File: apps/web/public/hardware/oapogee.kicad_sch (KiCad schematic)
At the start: 22 parts, among them J1 USB-C-16P, J2 S2B-PH-K-S, J3 ANT-902-928, U1 MCP73831, U2 TODO-BUCK-BOOST, U3 RP2350A, U4 W25Q128JVSIQ, U5 BMP390, U6 ICM-42688-P, U7 ADXL375, U8 SX1262, U9 MAX-M10S

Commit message: Fix 37 audited defects, wire the board's power, and make zoom crisp
A four-way audit with adversarial verification found 37 confirmed defects, seven
of them blockers. The verifier's job was to refute each finding, so what
survived is what could be proven from the files.

Specs. The STATUS pressure field's stated range did not follow from its own
encoding formula and matched no consistent reading of it, so two implementers
would have clamped and raised BARO_FAULT at different pressures. It is now
whole pascals offset by 50000, which covers 50000 to 115535 Pa in exactly 65536
codes, makes the "offset so it fits in 16 bits" rationale literally true, and
puts the packet and the log on the same pressure scale. The reference decoder
silently dropped the body of two of the five packet types, including the BEACON
that carries the apogee figure; it now covers all five. t_ms before arming,
POSITION with no fix, and the manifest summary's absent-versus-null
contradiction are all defined rather than left to the reader.

Content. The claim that an IMU saturates "around 16 g" above "a C motor" was
stated as fact in six rendered places while the part's own note admitted the
threshold had never been computed. The mechanism stays, because it is real and
worth explaining; the specific figures are now marked. Same for a stray range
figure of "a kilometre" on a site that says it publishes no range figures.

Hardware. The schematic had no GND net and no 3V3 net at all, so every supply
pin floated and the pull-ups the comments described pulled towards nothing. It
also had no arming input, while the state machine's first transition is
operator-driven, so the firmware had no signal to detect the event that starts
the log. Both are now wired, along with a battery sense divider, because the
packet format transmits a battery voltage that nothing on the board could have
measured.

Site. Two print blockers: the preflight checklist printed white on white with no
title, and closed tab panels were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
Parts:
- added GND (x14): GND, symbol Custom:rail_down
- added R6, R7, R8: 100kΩ, symbol Device:boxresistor_right
- added SW1: ARM-SWITCH, symbol Device:U_ARM-SWITCH
- added V3V3 (x12): V3V3, symbol Custom:rail_up
- added VBAT (x4): VBAT, symbol Custom:rail_up
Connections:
- net at C3.1: now also U2.4 (VOUT)
- net at R2.2: now also R1.2
- net at U9.2 (GND): now also J3.2 (GND)
- net at U2.2 (GND): now also C2.2
- net at C2.1: no longer U2.4 (VOUT)
- net at R4.2: now also R5.2
- net at U1.2 (VSS): now also R3.2
- net at D1.3 (GND): now also LS1.2 (GND)
- net GND: now reaches U3.2 (GND)
- net GND: now also J1.2 (GND)
- net U3_VBAT_SENSE: now reaches U3.25 (VBAT_SENSE)
- net U3_VBAT_SENSE: now also R7.2, R8.1
- net at U5.2 (GND): now also U5.5 (SDO)
- net at J2.2 (GND): now also C1.2
- net U1_VBAT: no longer names the net of C1.1, U2.1 (VIN)
- net U1_VBAT: no longer J2.1 (VBAT), U1.3 (VBAT)
- new net: J2.1 (VBAT), R7.1
- new net U3_ARM: R6.1, SW1.1 (A), U3.27 (ARM)

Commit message: Give the board a layout, and a verification process that says why it cannot be built
The schematic has been a connectivity diagram since the first commit: every part
carried schematic coordinates, none carried a footprint, and the board was
marked routingDisabled. There was nothing to fabricate and nothing that would
have told you so.

All 26 parts now have the footprint of their real package and a place on the
22 by 60 board, laid out deliberately: USB and the power chain at one end, the
microcontroller central, sensors below it, the radio and its antenna at the far
end away from the digital section, the arming switch on an edge where a thumb
can reach it. The site publishes the PCB and assembly views alongside the
schematic.

The board still cannot be fabricated, and the point of this commit is that the
repository now says so precisely rather than shipping a plausible-looking board.

tools/check-pcb.mjs reads the exported circuit JSON rather than trusting the
exporter, because `tsci export` prints success and exits zero having laid down
no copper at all. That is not hypothetical: it happened here twice for unrelated
reasons and neither was visible in an exit code or a file size.

The first cause came from reading ~/Projects/nband, which had already paid for
the diagnosis. tscircuit's default autorouter calls .map() on the Iterator from
Map.prototype.entries(), which is ES2025 Iterator Helpers and absent from the
Bun on this machine. Verified before adopting their polyfill: the one-liner
throws on Bun 1.1.18 here. The second cause was placement errors, which make
tscircuit skip routing entirely and mention it only inside the JSON.

Everything blocking the board traces to one root. U3 declares 27 pins against a
60 pad QFN, so pads collide at zero clearance, which produces 36 placement
errors, which makes tscircuit skip routing, which leaves 39 nets unrouted and 39
ports unconnected. The router itself is fine: with placement checks bypassed as
an experiment it laid 7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
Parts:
- removed GND (x14): GND, symbol Custom:rail_down
- removed V3V3 (x12): V3V3, symbol Custom:rail_up
- removed VBAT (x4): VBAT, symbol Custom:rail_up
- added GND (x13): GND, symbol Custom:rail_down
- added V3V3 (x11): V3V3, symbol Custom:rail_up
- added VBAT (x4): VBAT, symbol Custom:rail_up
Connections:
- net at C2.1: now also U2.4 (VOUT)
- net at U2.2 (GND): no longer C2.2
- net at U2.1 (VIN): now also U2.3 (EN); no longer C1.1
- net at C3.1: no longer U2.4 (VOUT)
- net at U6.1 (VDD): now also U5.1 (VDD)
- net at U6.2 (GND): now also U7.2 (GND)
- net U3_GNSS_RX: now reaches U3.22 (GNSS_RX), U9.3 (TXD)
- net U8_ANT: now reaches J3.1 (ANT), U8.9 (ANT)
- net U3_GNSS_TX: no longer names the net of U3.21 (GNSS_TX), U9.4 (RXD)

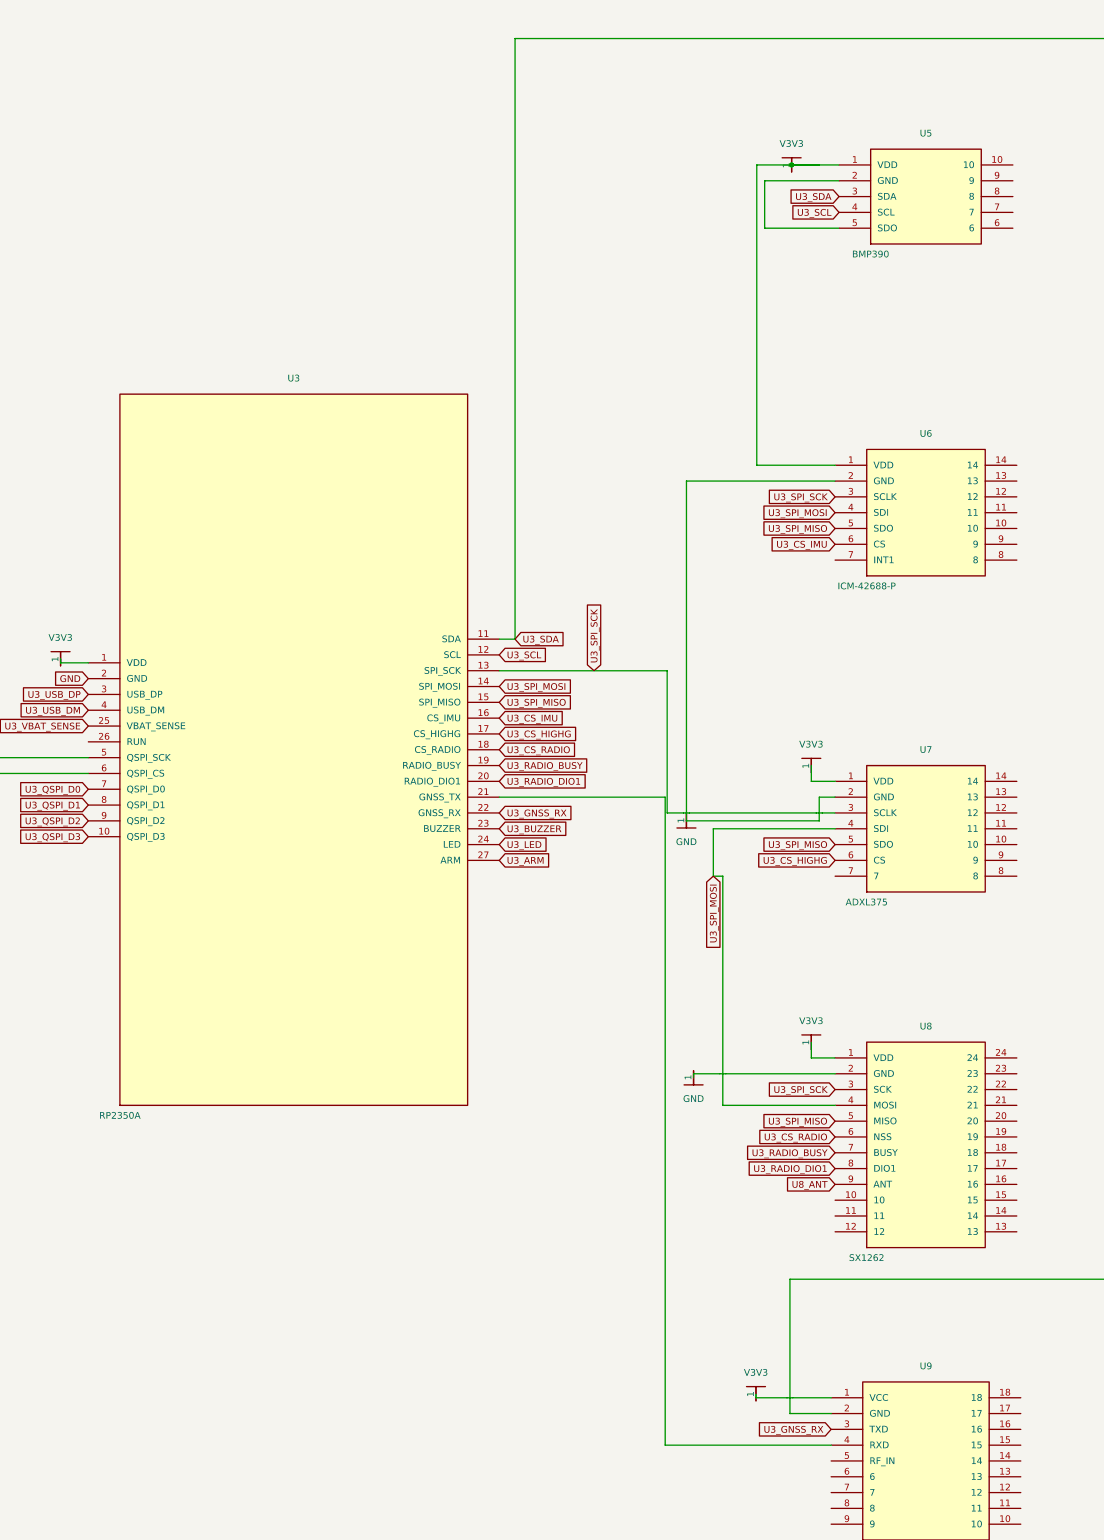
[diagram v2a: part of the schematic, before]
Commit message: Route the board
The RP2350's pinout is no longer a placeholder, and everything downstream of it
moved.

The 60 pins came from the Raspberry Pi datasheet, checked rather than taken on
trust: a community pinout gave one answer, and reconstructing the package
diagram on page 16 of RP-008373 gave the same answer pin for pin. That also
settled something the placeholder had hidden, which is that the part's ground is
the centre exposed pad and not a numbered pin at all. Signals are assigned to
GPIOs their peripherals can actually mux to: I2C0 on GPIO4 and 5, SPI0 on 16, 18
and 19, UART1 on 24 and 25, the battery sense on the one GPIO wired to the ADC.

Two things fell out of doing it properly. The core supply is an internal
switching regulator, and a switching regulator needs an external inductor, so L1
exists now and is in the bill of materials. It was absent for as long as the
pins that need it were absent, which is the kind of gap a placeholder hides: the
schematic looked complete without it.

And tscircuit's generic quad footprints are wrong. The corner pad of one side
overlaps the corner pad of the perpendicular side by about 0.14 mm, which is a
short between two pins, on every qfn and lga in the library, and no combination
of the pad-length and pad-width parameters changes it. Measured, not assumed:
the true minimum pad-to-pad gap on U3, U5 and U8 was 0.0000 mm. The land patterns
are built here now, numbered counter-clockwise from the top of the left side the
way the datasheet numbers the package, with the pads sitting outboard of the body
edge the way a real land pattern does. Minimum gap is 0.106 mm and up.

The board went from no copper at all to 95 routed traces, 134 vias, no missing
traces, no unconnected ports, no courtyard overlaps and no pad clearance errors.

One blocker remains and it is a real one. The measured copper-to-copper check
finds 55 pairs on the same layer, on different nets, closer than 0.127 mm, and
the closest is negative, which means they cro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
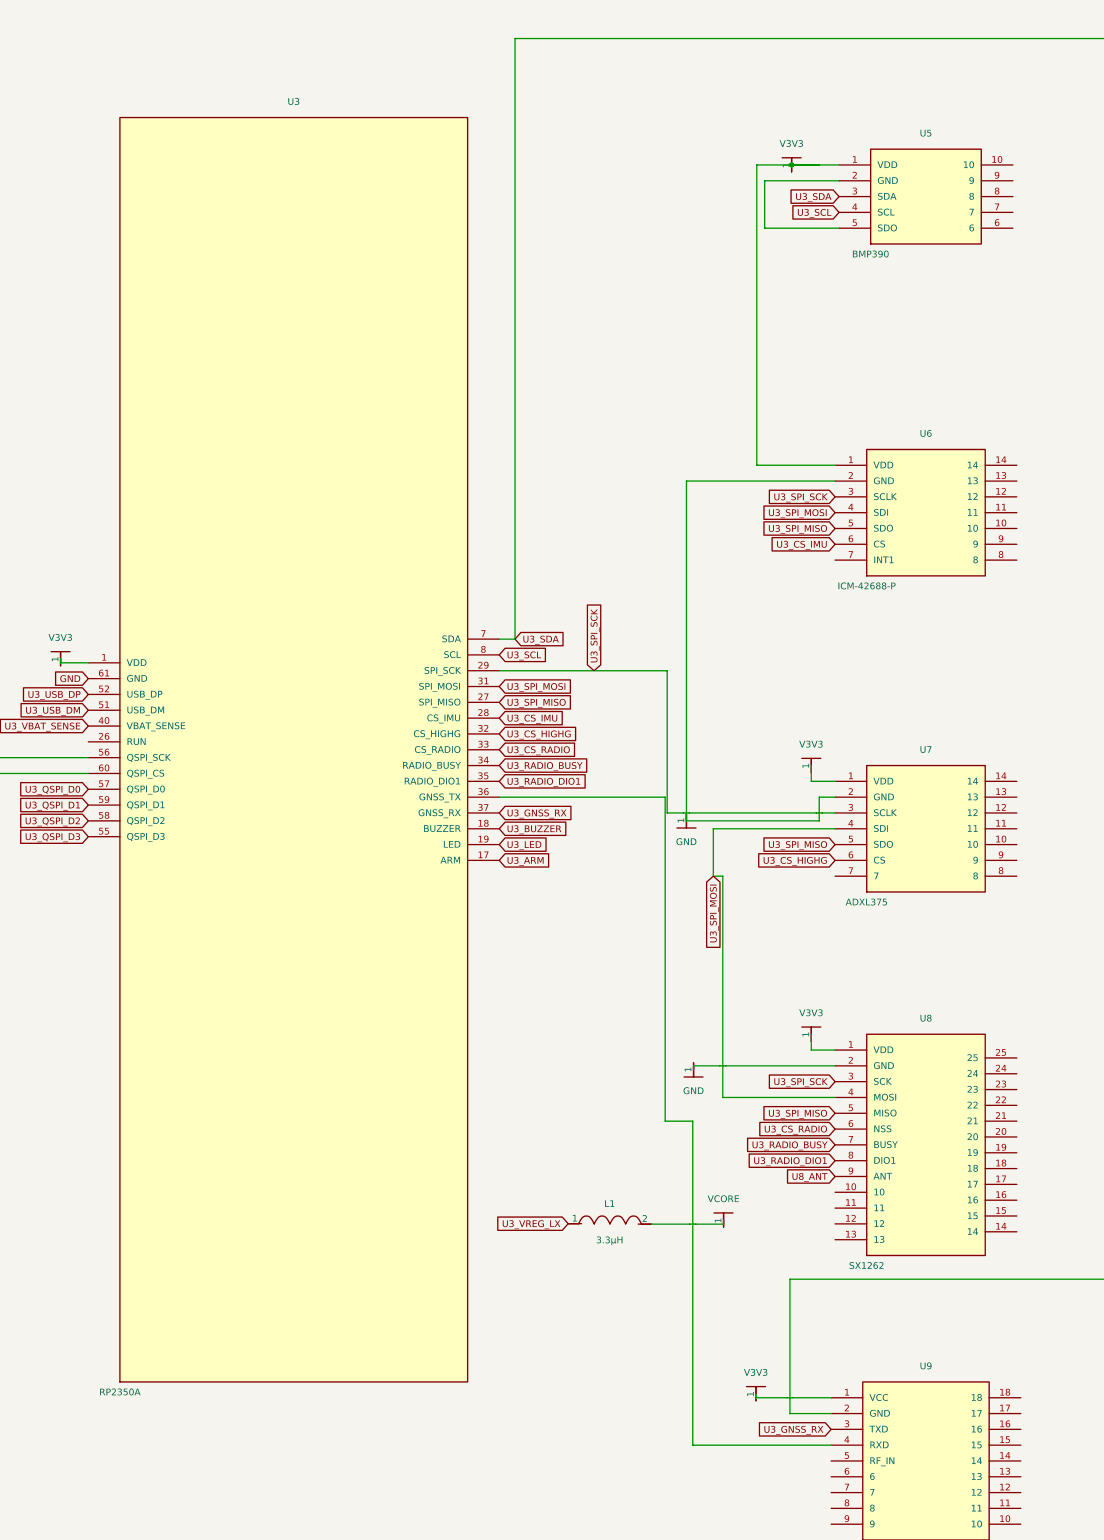
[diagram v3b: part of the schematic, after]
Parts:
- removed GND (x13): GND, symbol Custom:rail_down
- removed V3V3 (x11): V3V3, symbol Custom:rail_up
- removed VBAT (x4): VBAT, symbol Custom:rail_up
- added GND (x13): GND, symbol Custom:rail_down
- added L1: 3.3µH, symbol Device:inductor_right
- added V3V3 (x11): V3V3, symbol Custom:rail_up
- added VBAT (x4): VBAT, symbol Custom:rail_up
- added VCORE: VCORE, symbol Custom:rail_up
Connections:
- net GND: now also U3.61 (GND); no longer U3.2 (GND)
- net U3_ARM: now also U3.17 (ARM); no longer U3.27 (ARM)
- net U3_BUZZER: now also U3.18 (BUZZER); no longer U3.23 (BUZZER)
- net U3_CS_HIGHG: now also U3.32 (CS_HIGHG); no longer U3.17 (CS_HIGHG)
- net U3_CS_IMU: now also U3.28 (CS_IMU); no longer U3.16 (CS_IMU)
- net U3_CS_RADIO: now also U3.33 (CS_RADIO); no longer U3.18 (CS_RADIO)
- net U3_GNSS_RX: now also U3.37 (GNSS_RX); no longer U3.22 (GNSS_RX)
- net U3_LED: now also U3.19 (LED); no longer U3.24 (LED)
- net U3_QSPI_D0: now also U3.57 (QSPI_D0); no longer U3.7 (QSPI_D0)
- net U3_QSPI_D1: now also U3.59 (QSPI_D1); no longer U3.8 (QSPI_D1)
- net U3_QSPI_D2: now also U3.58 (QSPI_D2); no longer U3.9 (QSPI_D2)
- net U3_QSPI_D3: now also U3.55 (QSPI_D3); no longer U3.10 (QSPI_D3)
- net U3_RADIO_BUSY: now also U3.34 (RADIO_BUSY); no longer U3.19 (RADIO_BUSY)
- net U3_RADIO_DIO1: now also U3.35 (RADIO_DIO1); no longer U3.20 (RADIO_DIO1)
- net U3_SCL: now also U3.8 (SCL); no longer U3.12 (SCL)
- net U3_SDA: now also U3.7 (SDA); no longer U3.11 (SDA)
- net U3_SPI_MISO: now also U3.27 (SPI_MISO); no longer U3.15 (SPI_MISO)
- net U3_SPI_MOSI: now also U3.31 (SPI_MOSI); no longer U3.14 (SPI_MOSI)
- net U3_SPI_SCK: now also U3.29 (SPI_SCK); no longer U3.13 (SPI_SCK)
- net U3_USB_DM: now also U3.51 (USB_DM); no longer U3.4 (USB_DM)
- net U3_USB_DP: now also U3.52 (USB_DP); no longer U3.3 (USB_DP)
- net U3_VBAT_SENSE: now also U3.40 (VBAT_SENSE); no longer U3.25 (VBAT_SENSE)
- net at U4.1 (CS): now also U3.60 (QSPI_CS); no longer U3.6 (QSPI_CS)
- net at U4.6 (CLK): now also U3.56 (QSPI_SCK); no longer U3.5 (QSPI_SCK)
- net at U9.4 (RXD): now also U3.36 (GNSS_TX); no longer U3.21 (GNSS_TX)
- new net U3_VREG_LX: L1.1

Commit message: Verify the routed artifacts by source hash, not by bytes
CI failed on `oapogee-pcb.svg does not match the source` while the same command
passed locally. The autorouter is deterministic on one machine, checked by
rendering three times for an identical hash, and produces a different result on
CI's Linux than on macOS. A byte comparison of a routed board is therefore
asking the wrong question.

Dropping the comparison and checking nothing would be worse, because the mistake
that actually happens is editing the circuit and forgetting to re-render. So the
artifacts carry a hash of the source they came from, the same pattern the
printed parts already use, and CI verifies that instead. Confirmed it fails by
moving one component 0.1 mm and watching it complain.
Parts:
- removed GND (x13): GND, symbol Custom:rail_down
- removed V3V3 (x11): V3V3, symbol Custom:rail_up
- removed VBAT (x4): VBAT, symbol Custom:rail_up
- added GND (x13): GND, symbol Custom:rail_down
- added V3V3 (x11): V3V3, symbol Custom:rail_up
- added VBAT (x4): VBAT, symbol Custom:rail_up

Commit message: Record what was tried against the autorouter's shorts
The remaining blocker is 55 pairs of copper on the same layer, on different
nets, closer than a fab will build, and the closest is negative, meaning they
cross. Three attempts to make the router produce a clean board, all recorded in
the check's own message so the next person does not repeat them:

Raising autorouter traceClearance to 0.2 mm changed nothing. Identical trace
count, identical via count, identical 55 violations, so the setting is either
not reaching the router or not what it sounds like.

The sequential_trace preset lays no copper at all: 0 traces, 40 nets unrouted.

A four-layer board did not finish routing in ten minutes and was killed.

Before believing any of it I checked the checker rather than the router, because
a measurement that accuses a tool should be the first thing doubted. Route points
carry a layer and my comparison honours it. Same-net segments are excluded and
all 99 source traces resolve to a connectivity key, so nothing falls back to a
per-trace identity that would make one net look like many. Filtering vias out of
a route does not create phantom segments, because the via sits at the same
coordinates as the wire points either side of it. And one violation was worked
by hand: net1 from (-1.91, 5.94) to (-1.42, 6.44) genuinely intersects net9 from
(-0.14, 6.10) to (-2.90, 6.26) on the bottom layer.

So the finding stands and the gate stays shut. The board is fully placed, fully
routed, and one autorouter defect away from being orderable.
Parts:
- removed GND (x13): GND, symbol Custom:rail_down
- removed V3V3 (x11): V3V3, symbol Custom:rail_up
- removed VBAT (x4): VBAT, symbol Custom:rail_up
- added GND (x13): GND, symbol Custom:rail_down
- added V3V3 (x11): V3V3, symbol Custom:rail_up
- added VBAT (x4): VBAT, symbol Custom:rail_up

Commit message: The board is orderable
Fabrication blockers: none. `make fab` opened, and the repository now carries a
complete package: both copper layers, mask, paste and silkscreen on both sides,
edge cuts, plated and non-plated drill files, the bill of materials and the pick
and place. 27 components, 95 routed traces, 154 vias.

Two things got it there, and one of them was me being wrong.

The traces are 0.127 mm now. Clearance is centre distance minus half of each
width, so narrowing the copper buys clearance directly, and the router's own
internal margin turned out to be the binding constraint at about 0.115 mm no
matter what it was given. That was worth establishing rather than guessing at:
every local preset produces byte-identical results because they all resolve to
the same router; raising traceClearance changes nothing; the latest tscircuit,
thirteen releases newer, produces exactly the same 95 traces and 134 vias;
sequential_trace lays no copper; four layers did not finish in ten minutes; and
growing the board without moving the parts only adds margin around the same
congestion.

The other thing is the threshold. This refused to publish anything below
0.127 mm, a number inherited from a sibling project without ever being checked
against where this board would actually be made. PCBWay quotes 4 mil trace and
space as standard for two layers; JLCPCB quotes 5 mil at 1 oz copper. So a board
at 0.115 mm is not unmanufacturable, it is manufacturable at one of them and not
the other, and saying "no fab will build this" was simply false. There are two
sourced thresholds now: below 0.1 mm is a hard failure because no mainstream
standard process takes it, and between 0.1 and 0.127 is an advisory naming which
fab will take the order. That is a relaxation and it is recorded as one.

Two mistakes on the way, both caught by the checks. A regex meant to nudge a
component matched the thermal pad inside its own custom footprint instead,
moving the pad 8.7 mm off the board; tscircuit repo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
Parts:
- removed GND (x13): GND, symbol Custom:rail_down
- removed V3V3 (x11): V3V3, symbol Custom:rail_up
- removed VBAT (x4): VBAT, symbol Custom:rail_up
- added GND (x13): GND, symbol Custom:rail_down
- added V3V3 (x11): V3V3, symbol Custom:rail_up
- added VBAT (x4): VBAT, symbol Custom:rail_up
